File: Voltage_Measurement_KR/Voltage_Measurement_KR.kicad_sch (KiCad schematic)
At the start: 52 parts, among them IC1 MP9488GS-P, IC2 TLV1701AIDBVT, IC3 TLV1701AIDBVT, IC4 TLV1701AIDBVT, J1 Conn_01x02_Phoenix, J2 Conn_01x02_Phoenix, J3 Conn_01x03_Pin, J4 Conn_01x02_Pin, Q1 2N7000, Q2 2N7000, U1 HCPL-817-000E, U2 HCPL-817-000E, U3 HCPL-817-000E, U4 LM7805_SOT223

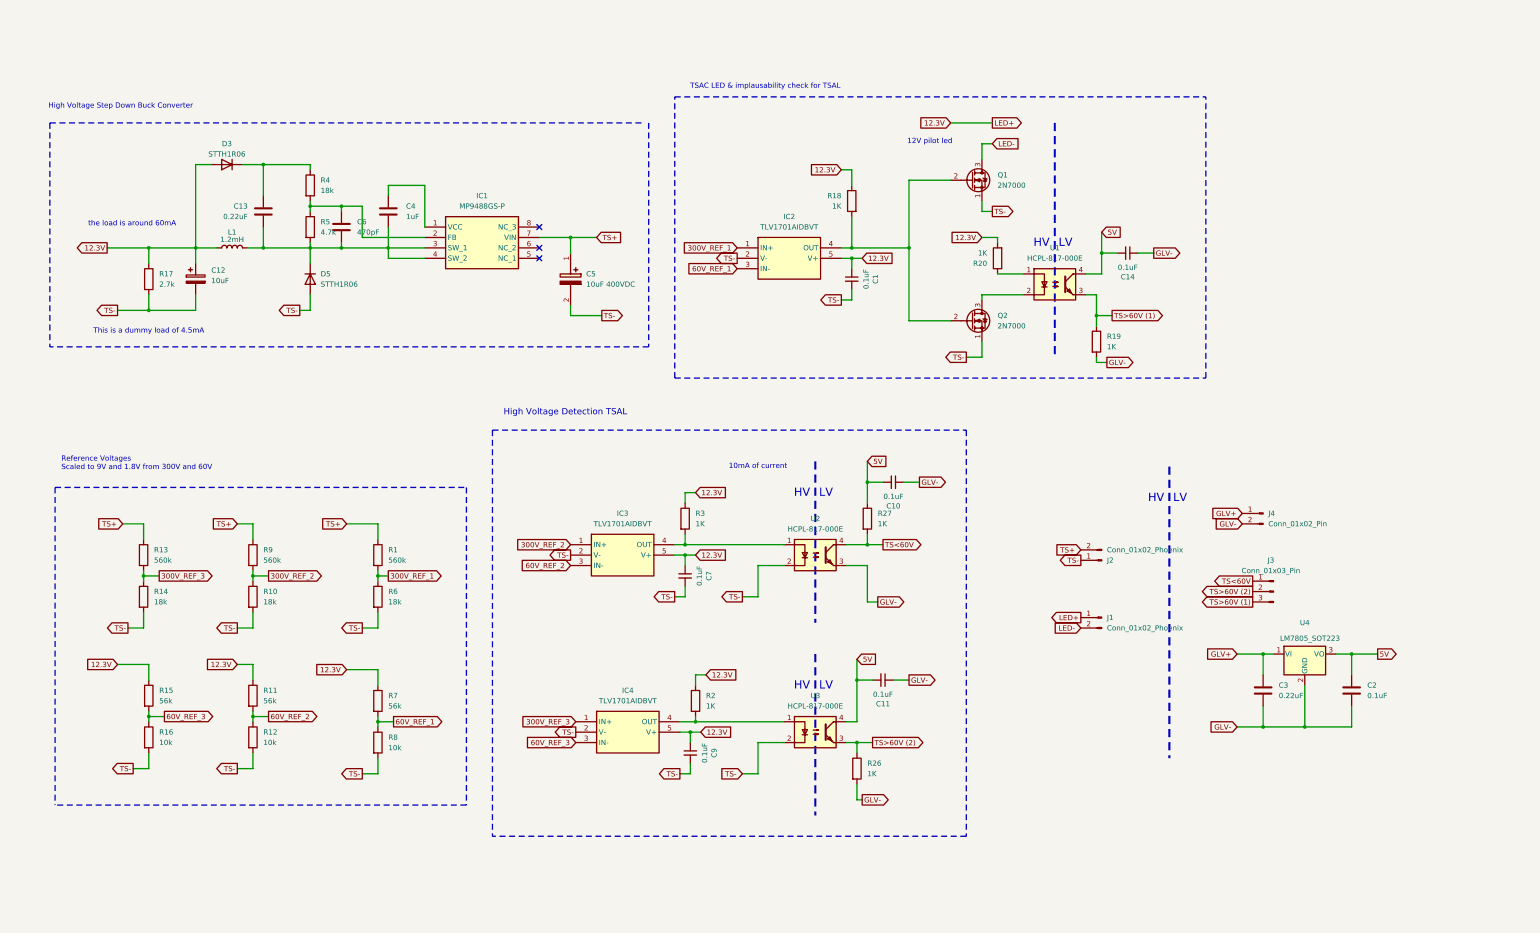
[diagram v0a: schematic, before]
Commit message: Voltage measurement completed
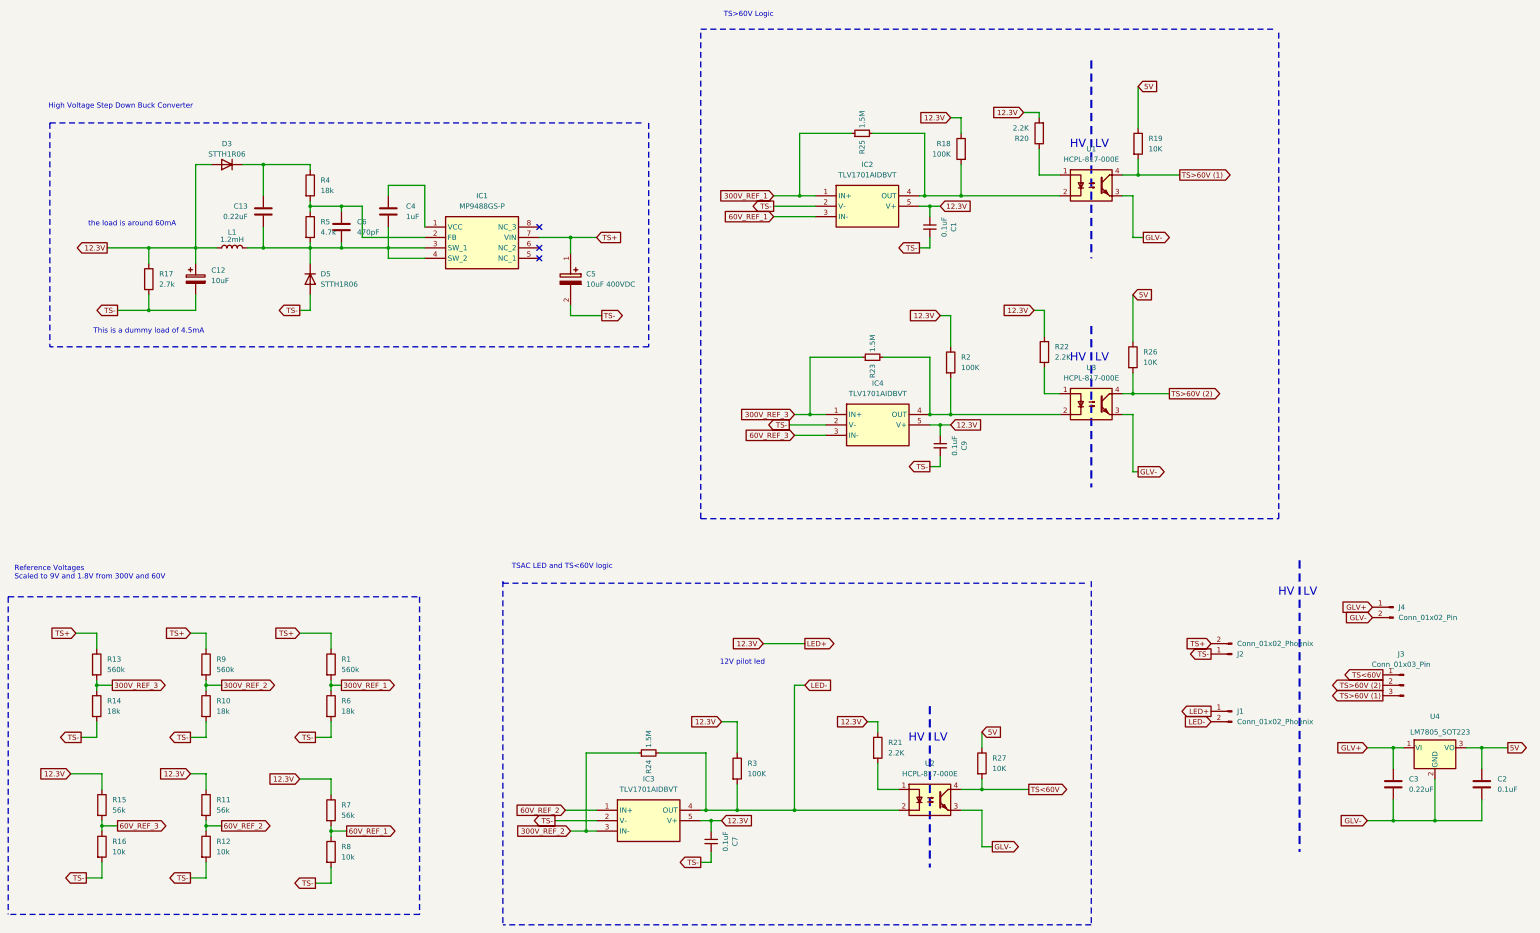
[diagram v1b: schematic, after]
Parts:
- removed C10, C11, C14: 0.1uF, FA14_Capacitor:FA18X7R1H104KNU00, symbol Device:C_Small
- removed Q1, Q2: 2N7000, Package_TO_SOT_THT:TO-92_Inline, symbol Transistor_FET:2N7000
- added R21, R22: 2.2K, Resistor_THT:R_Axial_DIN0207_L6.3mm_D2.5mm_P10.16mm_Horizontal, symbol Device:R
- added R23, R24, R25: 1.5M, Resistor_THT:R_Axial_DIN0207_L6.3mm_D2.5mm_P10.16mm_Horizontal, symbol Device:R_Small
- R18, R2, R3: value 1K -> 100K; Part number MCF 0.25W 1K -> MCF 0.25W 100K
- R19, R26, R27: value 1K -> 10K; Part number MCF 0.25W 1K -> MCF 0.25W 10K
- R20: value 1K -> 2.2K; Part number MCF 0.25W 1K -> MCF 0.25W 2.2K
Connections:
- net 12.3V: now also R21.1, R22.1
- net 300V_REF_1: now also R25.1
- net 300V_REF_2: now also IC3.3 (IN-), R24.1; no longer IC3.1 (IN+)
- net 300V_REF_3: now also R23.1
- net 5V: now also R19.1, R26.1; no longer U1.4, U3.4
- net 60V_REF_2: now also IC3.1 (IN+); no longer IC3.3 (IN-)
- net GLV-: now also U1.3, U3.3; no longer R19.2, R26.2
- net LED-: now also IC3.4 (OUT), R3.2, U2.2, R24.2
- net TS-: no longer U2.2, U3.2
- net TS>60V (1): now also R19.2, U1.4; no longer R19.1, U1.3
- net TS>60V (2): now also R26.2, U3.4; no longer R26.1, U3.3
- net at IC2.4 (OUT), R18.2: now also U1.2, R25.2
- net at IC4.4 (OUT), R2.2: now also U3.2, R23.2; no longer U3.1
- new net: R21.2, U2.1
- new net: R22.2, U3.1
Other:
- note added: "TS>60V Logic"
- note added: "TSAC LED and TS<60V logic"
- note removed: "10mA of current"
- note removed: "High Voltage Detection TSAL"
- note removed: "TSAC LED & implausability check for TSAL"
- moved on the sheet: C1, C2, C3, C7, C9, IC2, IC3, IC4, J1, J2, J3, J4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

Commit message: slave with new fuses added
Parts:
- R23, R24, R25: Part number (none) -> MCF 0.25W 1.5M
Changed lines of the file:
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@@
+			)
+		)
+		(property "Part number" "MCF 0.25W 1.5M"
+			(at 232.41 102.87 0)
+			(effects
+				(font
+					(size 1.27 1.27)
+				)
+				(hide yes)
 			)
 		)
@@
 			)
 		)
+		(property "Part number" "MCF 0.25W 1.5M"
+			(at 177.8 199.39 0)
+			(effects
+				(font
+					(size 1.27 1.27)
+				)
+				(hide yes)
+			)
+		)
 		(pin "1"
 		)
@@
 			(at 229.87 48.26 0)
 			(effects
+				(font
+					(size 1.27 1.27)
+				)
+				(hide yes)
+			)
+		)
+		(property "Part number" "MCF 0.25W 1.5M"
+			(at 229.87 48.26 0)
+			(effects

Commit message: added author
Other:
- company: (none) -> UCD Formula Student
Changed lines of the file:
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@@
 	(paper "A3")
 	(title_block
+		(company "UCD Formula Student")
 		(comment 1 "Author: Keelan Reilly")
 	)
